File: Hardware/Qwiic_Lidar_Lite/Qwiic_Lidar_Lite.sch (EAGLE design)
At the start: 12 parts, among them U1 XC9140

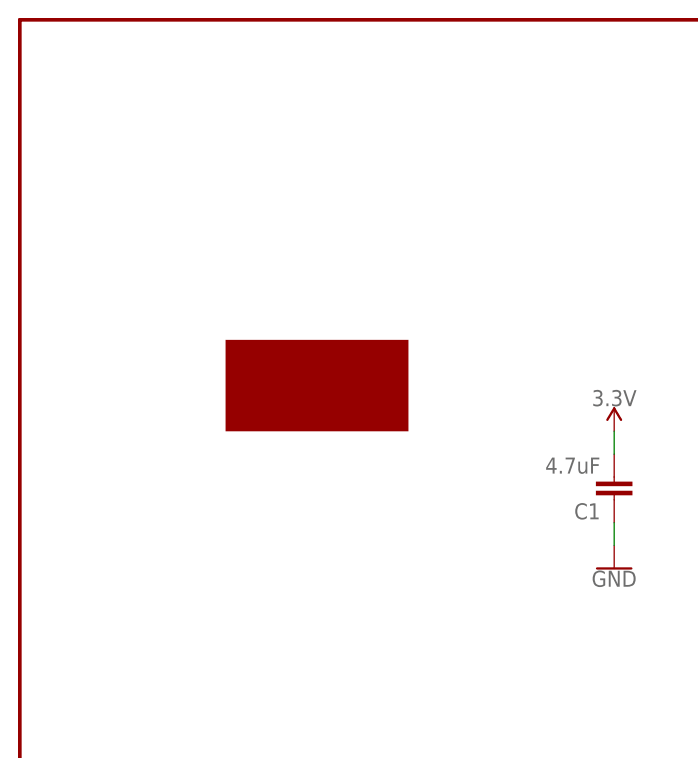
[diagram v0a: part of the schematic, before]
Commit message: Updated board design with power LED
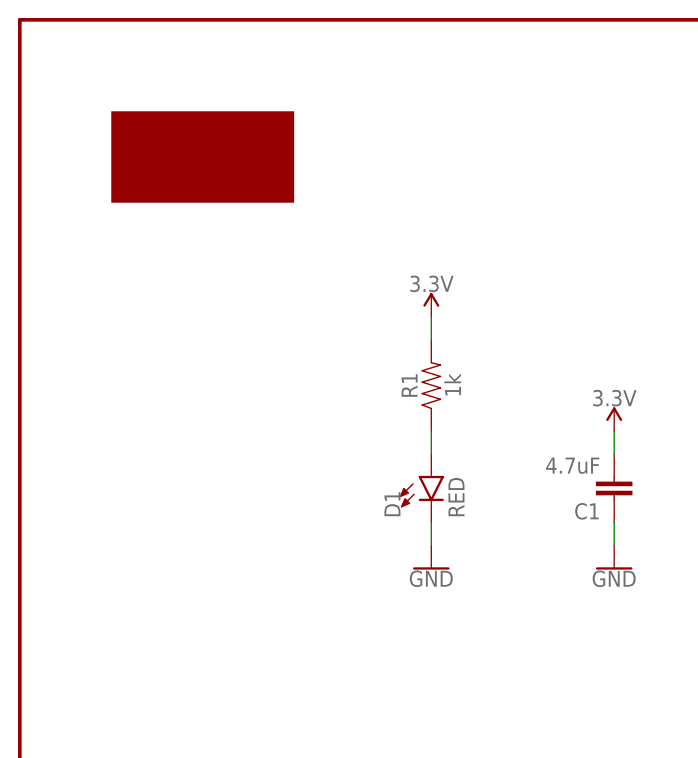
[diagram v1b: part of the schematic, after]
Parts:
- added D1: RED, SparkFun-LED:LED-RED0603
- added R1: 1k, SparkFun-Resistors:1KOHM-0603-1/10W-1%
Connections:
- new net N$1: D1.A, R1.1
- net 3.3V: now also R1.2
- net GND: now also D1.C
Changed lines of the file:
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@@
 <part name="J4" library="SparkFun-Connectors" deviceset="CONN_07" device="NO_SILK"/>
 <part name="SUPPLY10" library="SparkFun-PowerSymbols" deviceset="5V" device=""/>
+<part name="SUPPLY11" library="SparkFun-PowerSymbols" deviceset="3.3V" device=""/>
+<part name="D1" library="SparkFun-LED" deviceset="LED-RED" device="0603" value="RED"/>
+<part name="GND8" library="SparkFun-PowerSymbols" deviceset="GND" device=""/>
+<part name="R1" library="SparkFun-Resistors" deviceset="1KOHM" device="-0603-1/10W-1%" value="1k"/>
 </parts>
 <sheets>
@@
 <attribute name="VALUE" x="81.28" y="132.334" size="1.778" layer="96" align="bottom-center"/>
 </instance>
-<instance part="U$7" gate="G$1" x="33.02" y="144.78" smashed="yes"/>
+<instance part="U$7" gate="G$1" x="20.32" y="170.18" smashed="yes"/>
 <instance part="J2" gate="G$1" x="231.14" y="157.48" smashed="yes" rot="MR0">
 <attribute name="VALUE" x="236.22" y="152.146" size="1.778" layer="96" font="vector" rot="MR0" align="top-left"/>
@@
 <attribute name="VALUE" x="215.9" y="142.494" size="1.778" layer="96" align="bottom-center"/>
 </instance>
+<instance part="SUPPLY11" gate="G$1" x="45.72" y="152.4" smashed="yes">
+<attribute name="VALUE" x="45.72" y="155.194" size="1.778" layer="96" align="bottom-center"/>
+</instance>
+<instance part="D1" gate="G$1" x="45.72" y="134.62" smashed="yes">
+<attribute name="NAME" x="42.291" y="130.048" size="1.778" layer="95" font="vector" rot="R90"/>
+<attribute name="VALUE" x="47.625" y="130.048" size="1.778" layer="96" font="vector" rot="R90" align="top-left"/>
+</instance>
+<instance part="GND8" gate="1" x="45.72" y="124.46" smashed="yes">
+<attribute name="VALUE" x="45.72" y="124.206" size="1.778" layer="96" align="top-center"/>
+</instance>
+<instance part="R1" gate="G$1" x="45.72" y="144.78" smashed="yes" rot="R90">
+<attribute name="NAME" x="44.196" y="144.78" size="1.778" layer="95" font="vector" rot="R90" align="bottom-center"/>
+<attribute name="VALUE" x="47.244" y="144.78" size="1.778" layer="96" font="vector" rot="R90" align="top-center"/>
+</instance>
 </instances>
 <busses>
@@
 <wire x1="220.98" y1="124.46" x2="220.98" y2="119.38" width="0.1524" layer="91"/>
 <pinref part="GND6" gate="1" pin="GND"/>
+</segment>
+<segment>
+<pinref part="GND8" gate="1" pin="GND"/>
+<pinref part="D1" gate="G$1" pin="C"/>
+<wire x1="45.72" y1="127" x2="45.72" y2="129.54" width="0.1524" layer="91"/>
 </segment>
 </net>
@@
 <wire x1="220.98" y1="127" x2="223.52" y2="127" width="0.1524" layer="91"/>
 </segment>
+<segment>
+<pinref part="R1" gate="G$1" pin="2"/>
+<pinref part="SUPPLY11" gate="G$1" pin="3.3V"/>
+<wire x1="45.72" y1="149.86" x2="45.72" y2="152.4" width="0.1524" layer="91"/>
+</segment>
 </net>
 <net name="N$2" class="0">
@@
 </segment>
 </net>
+<net name="N$1" class="0">
+<segment>
+<pinref part="D1" gate="G$1" pin="A"/>
+<pinref part="R1" gate="G$1" pin="1"/>
+<wire x1="45.72" y1="137.16" x2="45.72" y2="139.7" width="0.1524" layer="91"/>
+</segment>
+</net>

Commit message: Stuff and things
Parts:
- added LOGO2: OSHW-LOGOMINI, SparkFun-Aesthetics:OSHW-LOGOMINI
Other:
- note added: "5V Boost"
- note added: "GARMIN mechanical outline"
- note added: "Power LED"
- note added: "Priyanka Makin"
- note added: "x01"
- moved on the sheet: C1, C2, D1, J1, J2, J3, J4, L1, R1, U1
